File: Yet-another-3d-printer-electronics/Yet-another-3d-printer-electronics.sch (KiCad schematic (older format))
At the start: 29 parts, among them CON1 SD_Card, P1 USB_B, P2 BEDTEMP, P3 ENDTEMP, P4 X-ENDSTOP, P5 Y-ENDSTOP, P6 Z-ENDSTOP, SW1 Switch_DPST, U1 FT230XS, U2 LPC1114FBD48/302, X1 CRYSTAL_SMD

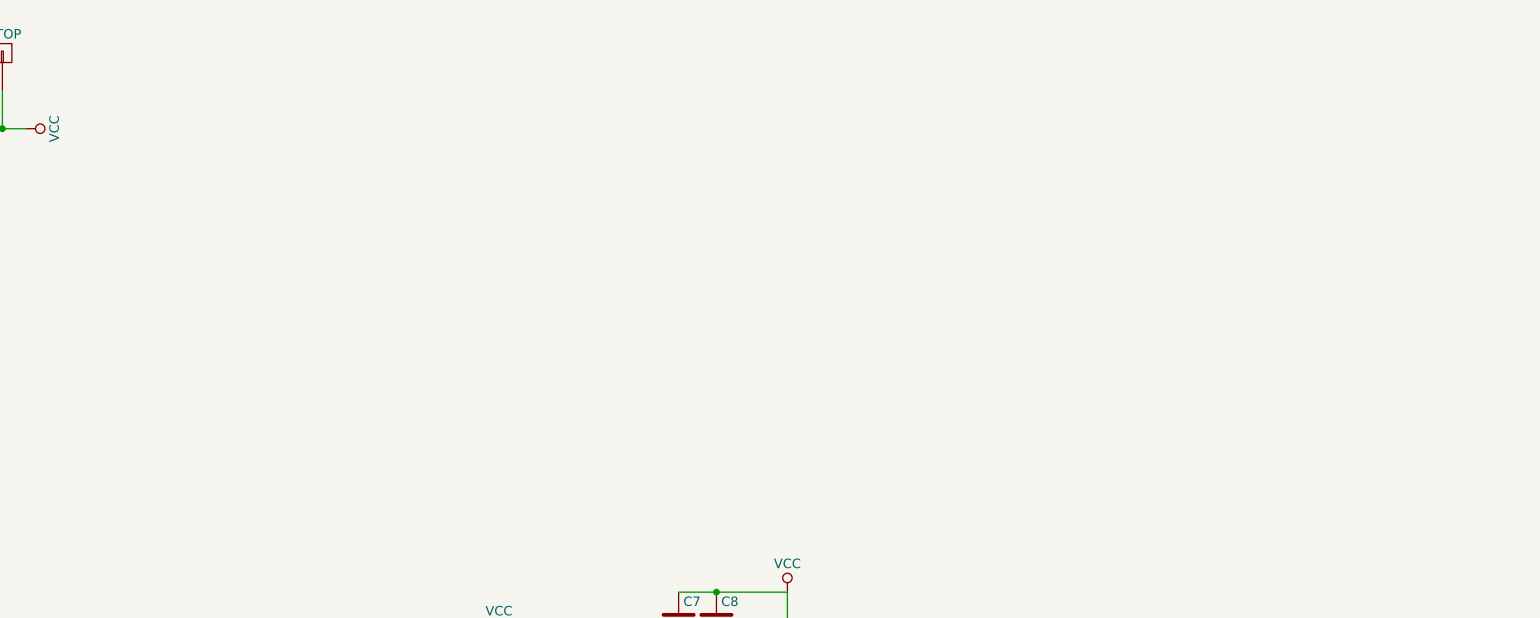
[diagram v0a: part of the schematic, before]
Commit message: Add extruder and hotbed heater, Fan
Signed-off-by: Mateusz Krawczuk <mat.krawczuk@gmail.com>
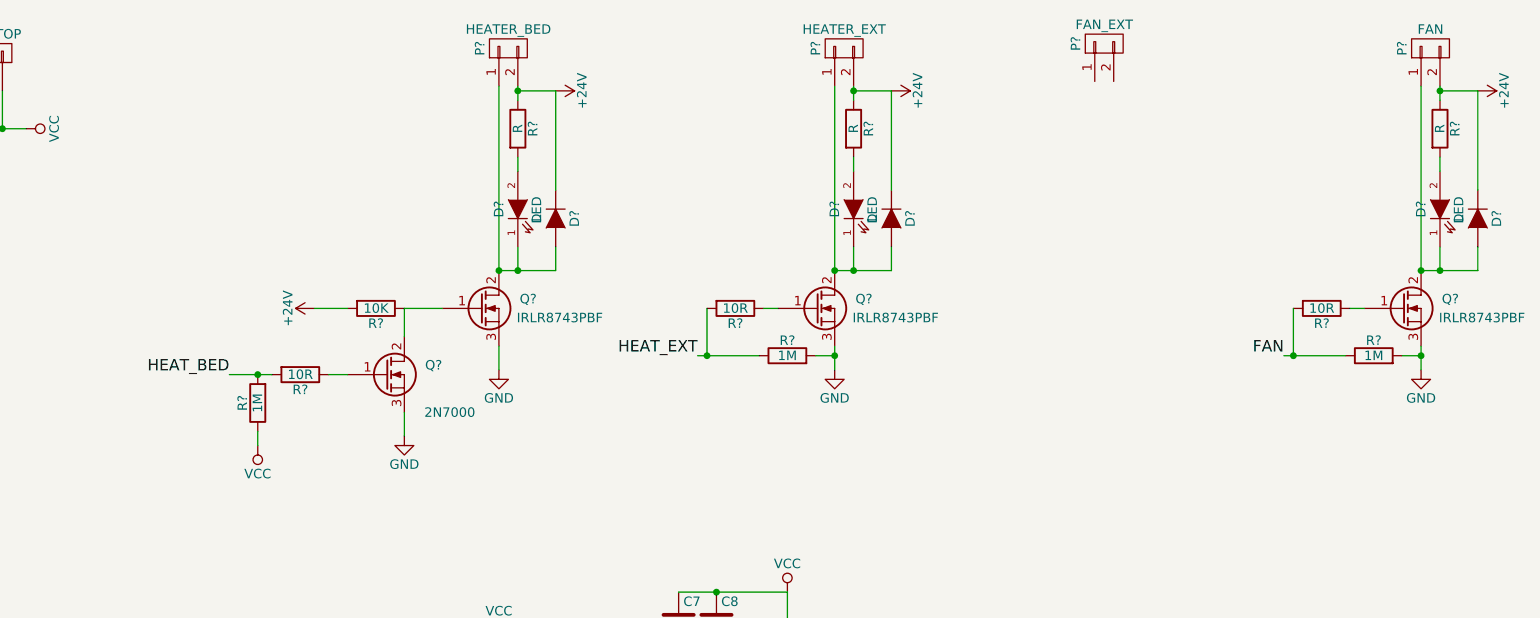
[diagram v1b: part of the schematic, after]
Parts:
- added D? (x3): D, symbol D
- added D? (x3): LED, symbol LED
- added P?: HEATER_BED, symbol CONN_01X02
- added P?: HEATER_EXT, symbol CONN_01X02
- added P?: FAN_EXT, symbol CONN_01X02
- added P?: FAN, symbol CONN_01X02
- added Q? (x3): IRLR8743PBF, symbol Q_NMOS_GDS
- added Q?: 2N7000, symbol Q_NMOS_GDS
- added R? (x3): R, symbol R
- added R?: 10K, symbol R
- added R? (x3): 10R, symbol R
- added R? (x3): 1M, symbol R
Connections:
- net GND: now also Q?.3 (S), Q?.3 (S), Q?.3 (S), Q?.3 (S), R?.2, R?.2
- net VCC: now also R?.1
- new net: Q?.1 (G), Q?.2 (D), R?.1
- new net: D?.1 (K), D?.2 (A), P?.1 (P1), Q?.2 (D) (x3)
- new net: D?.2 (A), R?.2 (x3)
- new net: Q?.1 (G), R?.1 (x3)
- new net +24V: D?.1 (K), D?.1 (K), D?.1 (K), P?.2 (P2), P?.2 (P2), P?.2 (P2), R?.1, R?.1, R?.1, R?.2
- new net FAN: R?.1, R?.2
- new net HEAT_BED: R?.2, R?.2
- new net HEAT_EXT: R?.1, R?.2

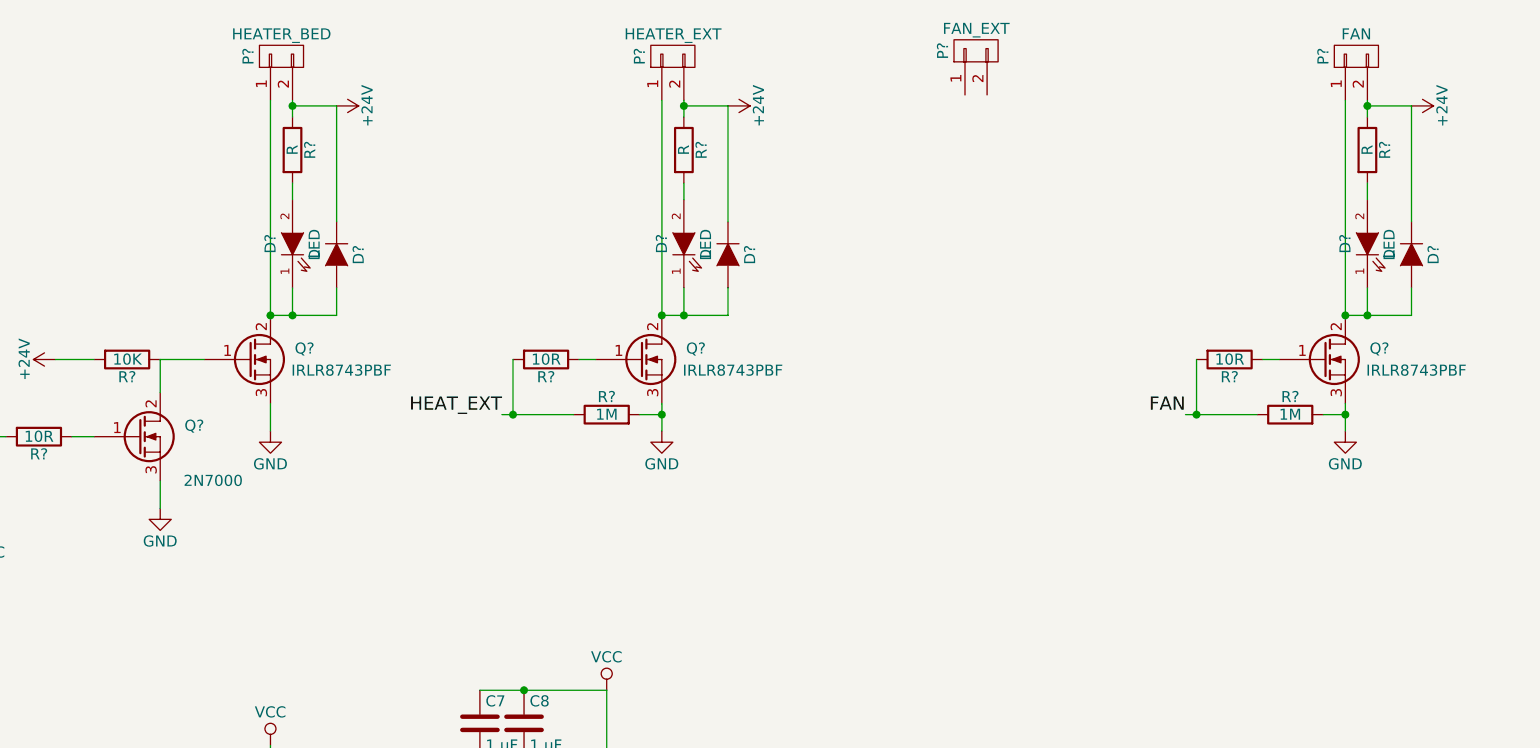
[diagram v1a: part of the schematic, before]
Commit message: Change mosfet for fan and add heater_fan
IRLR8743 is replaced by IRLML0030TRPbF for fans.

Signed-off-by: Mateusz Krawczuk <mat.krawczuk@gmail.com>
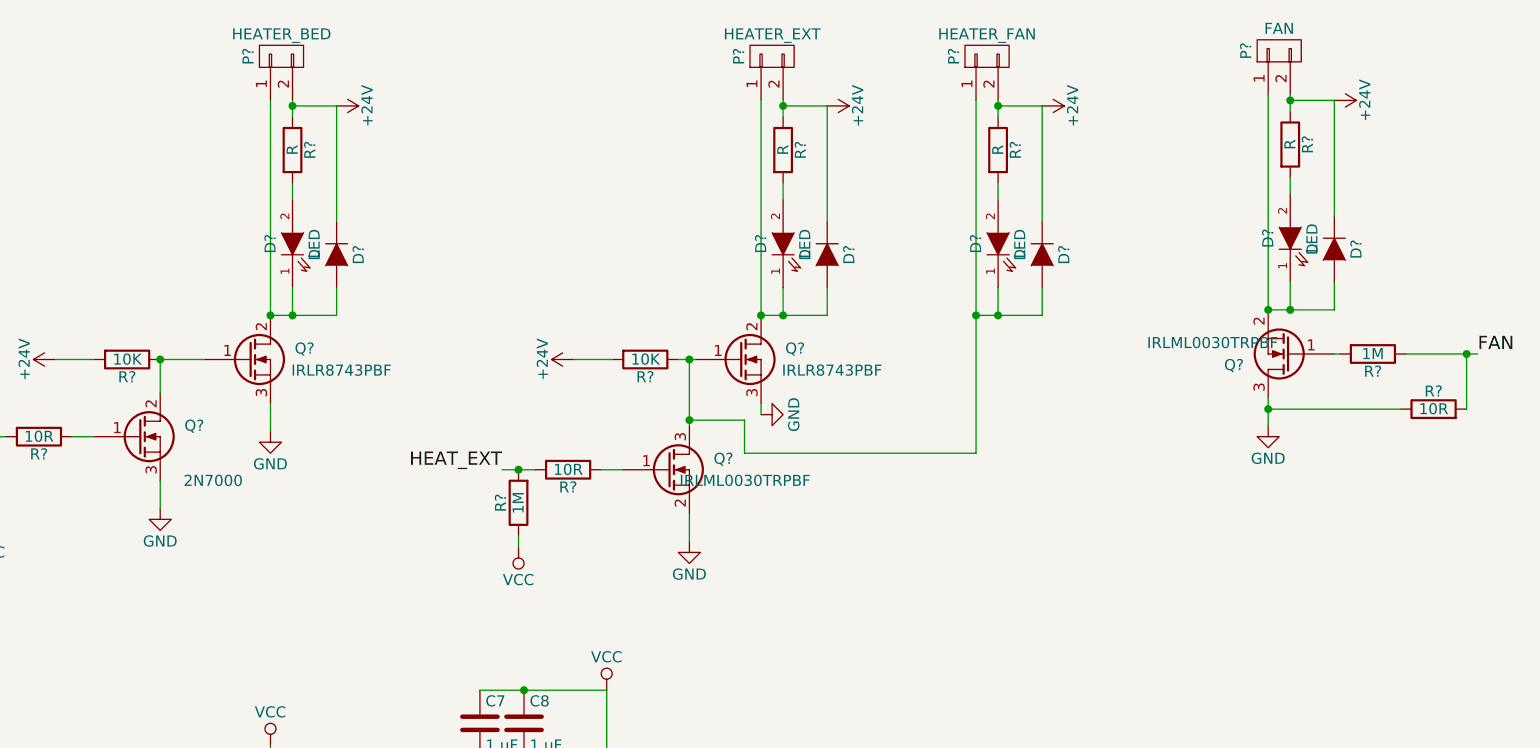
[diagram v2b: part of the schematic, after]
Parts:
- removed P?: FAN_EXT, symbol CONN_01X02
- removed Q?: IRLR8743PBF, symbol Q_NMOS_GDS
- removed R?: 1M, symbol R
- added D?: D, symbol D
- added D?: LED, symbol LED
- added P?: HEATER_FAN, symbol CONN_01X02
- added Q? (x2): IRLML0030TRPBF, symbol Q_NMOS_GSD
- added R?: R, symbol R
- added R?: 10R, symbol R
- added R?: 1M, symbol R
- R?: value 10R -> 10K
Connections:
- net +24V: now also R?.2, D?.1 (K), P?.2 (P2), R?.1
- net GND: now also R?.1, Q?.2 (S), Q?.3 (D); no longer R?.2
- net HEAT_EXT: now also R?.2, R?.2; no longer R?.2
- net VCC: now also R?.1
- net at D?.1 (K), D?.2 (A), P?.1 (P1): now also Q?.2 (S)
- net at Q?.1 (G), R?.1: now also D?.1 (K), D?.2 (A), P?.1 (P1), Q?.3 (D)
- new net: Q?.1 (G), R?.2
- new net: D?.2 (A), R?.2
- new net: Q?.1 (G), R?.1
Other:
- moved on the sheet: D?, P?, Q?, R?

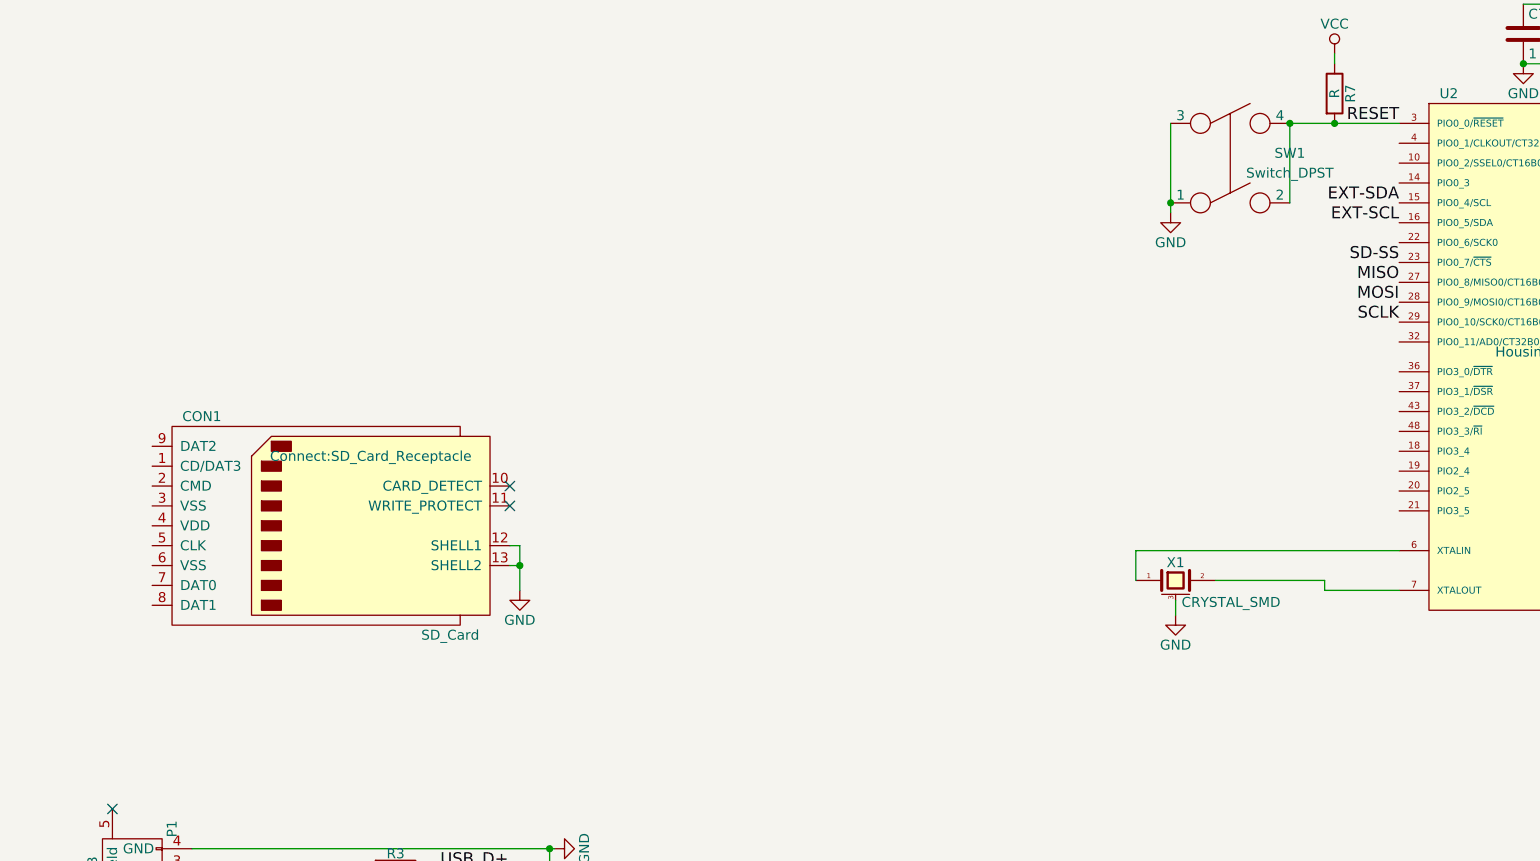
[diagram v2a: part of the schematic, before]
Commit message: Add sdcard connection
Signed-off-by: Mateusz Krawczuk <mat.krawczuk@gmail.com>
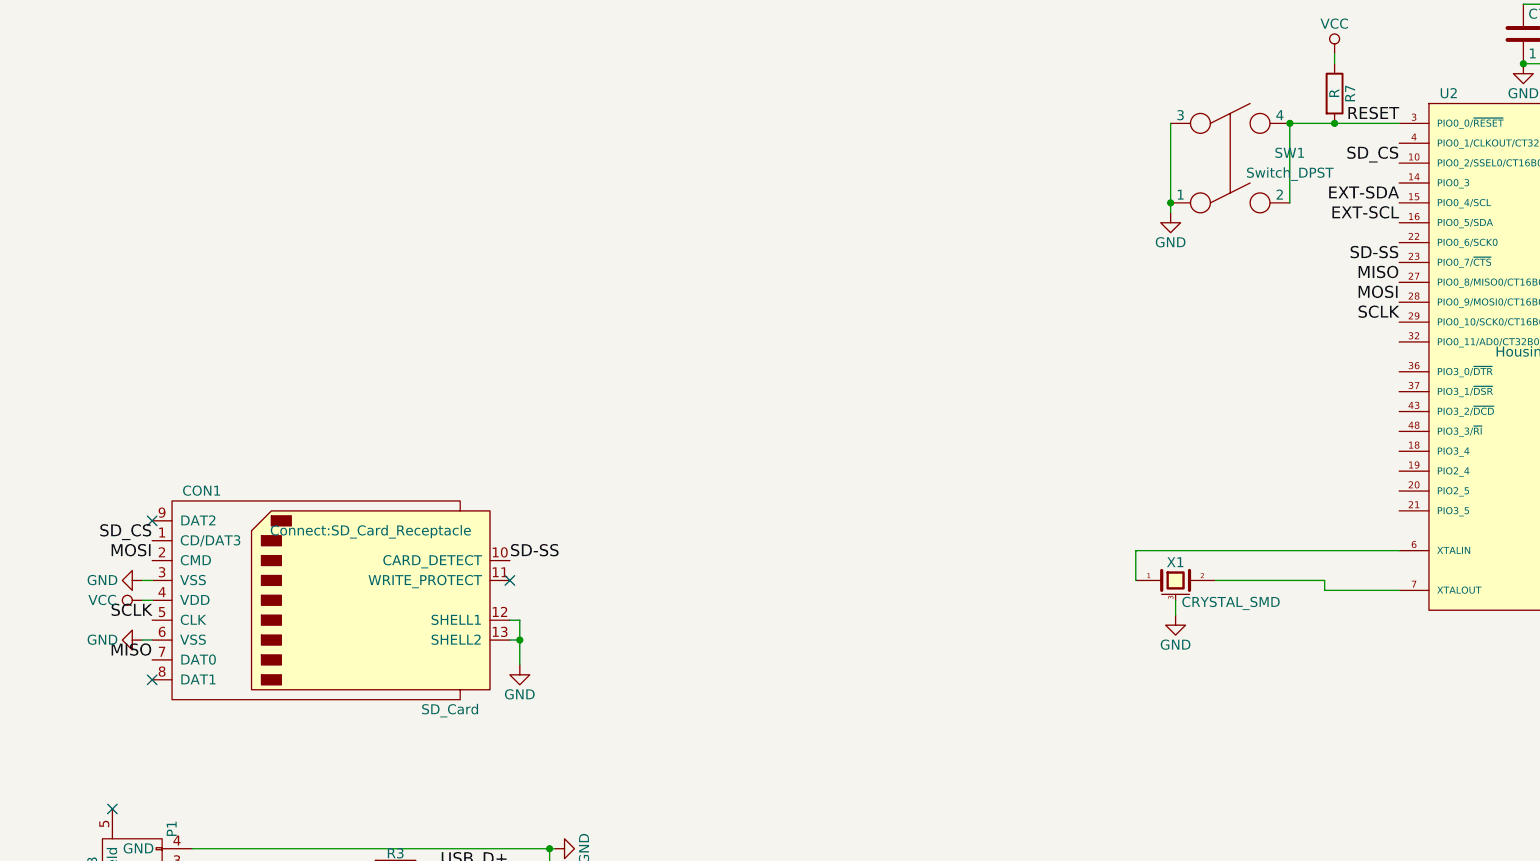
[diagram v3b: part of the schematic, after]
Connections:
- net GND: now also CON1.3 (VSS), CON1.6 (VSS)
- net MISO: now also CON1.7 (DAT0)
- net MOSI: now also CON1.2 (CMD)
- net SCLK: now also CON1.5 (CLK)
- net SD-SS: now also CON1.10 (CARD_DETECT)
- net VCC: now also CON1.4 (VDD)
- net SD_CS: now reaches U2.10 (PIO0_2/SSEL0/CT16B0_CAP0)
- net SD_CS: now also CON1.1 (CD/DAT3)
- no-connect marks 7 -> 8
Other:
- moved on the sheet: CON1
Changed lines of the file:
@@
 L SD_Card CON1
 U 1 1 588D063B
-P 2150 6200
-F 0 "CON1" H 1500 6750 50  0000 C CNN
-F 1 "SD_Card" H 2750 5650 50  0000 C CNN
-F 2 "Connect:SD_Card_Receptacle" H 2350 6550 50  0000 C CNN
-F 3 "" H 2150 6200 50  0000 C CNN
-	1    2150 6200
+P 2150 6575
+F 0 "CON1" H 1500 7125 50  0000 C CNN
+F 1 "SD_Card" H 2750 6025 50  0000 C CNN
+F 2 "Connect:SD_Card_Receptacle" H 2350 6925 50  0000 C CNN
+F 3 "" H 2150 6575 50  0000 C CNN
+	1    2150 6575
 	1    0    0    -1
 $EndComp
@@
 Text Label 4375 1200 3    60   ~ 0
 ENDSTOP-Z
-NoConn ~ 3050 6000
-NoConn ~ 3050 6100
+NoConn ~ 3050 6475
 $Comp
 L GND #PWR020
 U 1 1 588EF0E4
-P 3100 6525
-F 0 "#PWR020" H 3100 6275 50  0001 C CNN
-F 1 "GND" H 3100 6375 50  0000 C CNN
-F 2 "" H 3100 6525 50  0000 C CNN
-F 3 "" H 3100 6525 50  0000 C CNN
-	1    3100 6525
+P 3100 6900
+F 0 "#PWR020" H 3100 6650 50  0001 C CNN
+F 1 "GND" H 3100 6750 50  0000 C CNN
+F 2 "" H 3100 6900 50  0000 C CNN
+F 3 "" H 3100 6900 50  0000 C CNN
+	1    3100 6900
 	1    0    0    -1
 $EndComp
@@
 	4375 925  4375 1200
 Wire Wire Line
-	3050 6300 3100 6300
-Wire Wire Line
-	3100 6300 3100 6525
-Wire Wire Line
-	3050 6400 3100 6400
-Connection ~ 3100 6400
+	3050 6675 3100 6675
+Wire Wire Line
+	3100 6675 3100 6900
+Wire Wire Line
+	3050 6775 3100 6775
+Connection ~ 3100 6775
 Wire Wire Line
 	7500 1875 7500 1750
@@
 Wire Wire Line
 	8325 2925 8325 2875
+$Comp
+L GND #PWR?
+U 1 1 5890B49A
+P 1200 6475
+F 0 "#PWR?" H 1200 6225 50  0001 C CNN
+F 1 "GND" V 1200 6275 50  0000 C CNN
+F 2 "" H 1200 6475 50  0000 C CNN
+F 3 "" H 1200 6475 50  0000 C CNN
+	1    1200 6475
+	0    1    1    0
+$EndComp
+Wire Wire Line
+	1250 6475 1200 6475
+$Comp
+L VCC #PWR?
+U 1 1 5890C3D7
+P 1200 6575
+F 0 "#PWR?" H 1200 6425 50  0001 C CNN
+F 1 "VCC" V 1200 6775 50  0000 C CNN
+F 2 "" H 1200 6575 50  0000 C CNN
+F 3 "" H 1200 6575 50  0000 C CNN
+	1    1200 6575
+	0    -1   -1   0
+$EndComp
+Wire Wire Line
+	1250 6575 1200 6575
+Text Label 1250 6875 2    60   ~ 0
+MISO
+Text Label 1250 6375 2    60   ~ 0
+MOSI
+Text Label 1250 6675 2    60   ~ 0
+SCLK
+Text Label 3050 6375 0    60   ~ 0
+SD-SS
+$Comp
+L GND #PWR?
+U 1 1 5890D76C
+P 1200 6775
+F 0 "#PWR?" H 1200 6525 50  0001 C CNN
+F 1 "GND" V 1200 6575 50  0000 C CNN
+F 2 "" H 1200 6775 50  0000 C CNN
+F 3 "" H 1200 6775 50  0000 C CNN
+	1    1200 6775
+	0    1    1    0
+$EndComp
+Wire Wire Line
+	1250 6775 1200 6775
+NoConn ~ 1250 6175
+NoConn ~ 1250 6975
+Text Label 7525 4375 2    60   ~ 0
+SD_CS
+Text Label 1250 6275 2    60   ~ 0
+SD_CS
 $EndSCHEMATC

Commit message: Add stepstick component
Signed-off-by: Mateusz Krawczuk <mat.krawczuk@gmail.com>
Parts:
- added U?: X-Motor, symbol StepStick
- added U?: Y-Motor, symbol StepStick
- added U?: Z-Motor, symbol StepStick
- added U?: E-Motor, symbol StepStick
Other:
- moved on the sheet: C7, C8, D?, P?, Q?, R7, R?, SW1, U2, X1

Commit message: Add stepstick and motor sockets to schematics.
Stepstick have optional protection with Schottky diodes.

Signed-off-by: Mateusz Krawczuk <mat.krawczuk@gmail.com>
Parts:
- added 100K, 100K? (x3): R, symbol R
- added 10u/30V, 10u/30V? (x3): C, symbol C
- added C? (x4): CP, symbol CP
- added D? (x32): D_Schottky, symbol D_Schottky
- added P?: X-microsteps, symbol CONN_02X03
- added P?: X-Motor, symbol CONN_01X04
- added P?: Y-microsteps, symbol CONN_02X03
- added P?: Z-microsteps, symbol CONN_02X03
- added P?: E-microsteps, symbol CONN_02X03
- added P?: Y-Motor, symbol CONN_01X04
- added P? (x2): Z-Motor, symbol CONN_01X04
- added R? (x4): 10K, symbol R
- U?: value X-Motor -> X-Stepstick
- U?: value Y-Motor -> Y-Stepstick
- U?: value Z-Motor -> Z-Stepstick
- U?: value E-Motor -> E-Stepstick
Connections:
- net +24V: now also U?.16 (VMOT), U?.16 (VMOT), U?.16 (VMOT), U?.16 (VMOT), 10u/30V.1, 10u/30V?.1, 10u/30V?.1, 10u/30V?.1, C?.1, C?.1, C?.1, C?.1, D?.1 (K), D?.1 (K), D?.1 (K), D?.1 (K), D?.1 (K), D?.1 (K), D?.1 (K), D?.1 (K), D?.1 (K), D?.1 (K), D?.1 (K), D?.1 (K), D?.1 (K), D?.1 (K), D?.1 (K), D?.1 (K)
- net GND: now also U?.15 (GND_M), U?.15 (GND_M), U?.15 (GND_M), U?.15 (GND_M), U?.9 (VSS), U?.9 (VSS), U?.9 (VSS), U?.9 (VSS), 100K.1, 100K?.1, 100K?.1, 100K?.1, 10u/30V.2, 10u/30V?.2, 10u/30V?.2, 10u/30V?.2, C?.2, C?.2, C?.2, C?.2, D?.2 (A), D?.2 (A), D?.2 (A), D?.2 (A), D?.2 (A), D?.2 (A), D?.2 (A), D?.2 (A), D?.2 (A), D?.2 (A), D?.2 (A), D?.2 (A), D?.2 (A), D?.2 (A), D?.2 (A), D?.2 (A)
- net VCC: now also U?.10 (VDD), U?.10 (VDD), U?.10 (VDD), U?.10 (VDD), P?.1 (P1), P?.1 (P1), P?.1 (P1), P?.1 (P1), P?.3 (P3), P?.3 (P3), P?.3 (P3), P?.3 (P3), P?.5 (P5), P?.5 (P5), P?.5 (P5), P?.5 (P5), R?.1, R?.1, R?.1, R?.1
- net XYE_ENABLE: now reaches U?.1 (~ENABLE)
- net XYE_ENABLE: now also U?.1 (~ENABLE), U?.1 (~ENABLE), R?.2, R?.2, R?.2
- net at U?.11 (1B): now also D?.1 (K), D?.2 (A), P?.4 (P4) (x4)
- net at U?.12 (1A): now also D?.1 (K), D?.2 (A), P?.3 (P3) (x4)
- net at U?.13 (2A): now also D?.1 (K), D?.2 (A), P?.2 (P2) (x4)
- net at U?.14 (2B): now also D?.1 (K), D?.2 (A), P?.1 (P1) (x4)
- net X-MS1: now reaches U?.2 (MS1)
- net X-MS1: now also P?.6 (P6)
- net X-MS2: now reaches U?.3 (MS2)
- net X-MS2: now also P?.4 (P4)
- net X-MS3: now reaches U?.4 (MS3)
- net X-MS3: now also 100K.2, P?.2 (P2)
- net at U?.5 (~RESET): now also U?.6 (~SLEEP) (x4)
- net X-STEP: now reaches U?.7 (STEP)
- net X-DIR: now reaches U?.8 (DIR)
- net Y-MS1: now reaches U?.2 (MS1)
- net Y-MS1: now also P?.6 (P6)
- net Y-MS2: now reaches U?.3 (MS2)
- net Y-MS2: now also P?.4 (P4)
- net Y-MS3: now reaches U?.4 (MS3)
- net Y-MS3: now also 100K?.2, P?.2 (P2)
- net Y-STEP: now reaches U?.7 (STEP)
- net Y-DIR: now reaches U?.8 (DIR)
- net Z_ENABLE: now reaches U?.1 (~ENABLE)
- net Z_ENABLE: now also R?.2
- net Z-MS1: now reaches U?.2 (MS1)
- net Z-MS1: now also P?.6 (P6)
- net Z-MS2: now reaches U?.3 (MS2)
- net Z-MS2: now also P?.4 (P4)
- net Z-MS3: now reaches U?.4 (MS3)
- net Z-MS3: now also 100K?.2, P?.2 (P2)
- net Z-STEP: now reaches U?.7 (STEP)
- net Z-DIR: now reaches U?.8 (DIR)
- net E-MS1: now reaches U?.2 (MS1)
- net E-MS1: now also P?.6 (P6)
- net E-MS2: now reaches U?.3 (MS2)
- net E-MS2: now also P?.4 (P4)
- net E-MS3: now reaches U?.4 (MS3)
- net E-MS3: now also 100K?.2, P?.2 (P2)
- net E-STEP: now reaches U?.7 (STEP)
- net E-DIR: now reaches U?.8 (DIR)
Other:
- moved on the sheet: C7, C8, D?, P?, Q?, R7, R?, SW1, U2, U?, X1
